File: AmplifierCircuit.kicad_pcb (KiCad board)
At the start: 2 copper layers, 69 x 38 mm, 29 parts

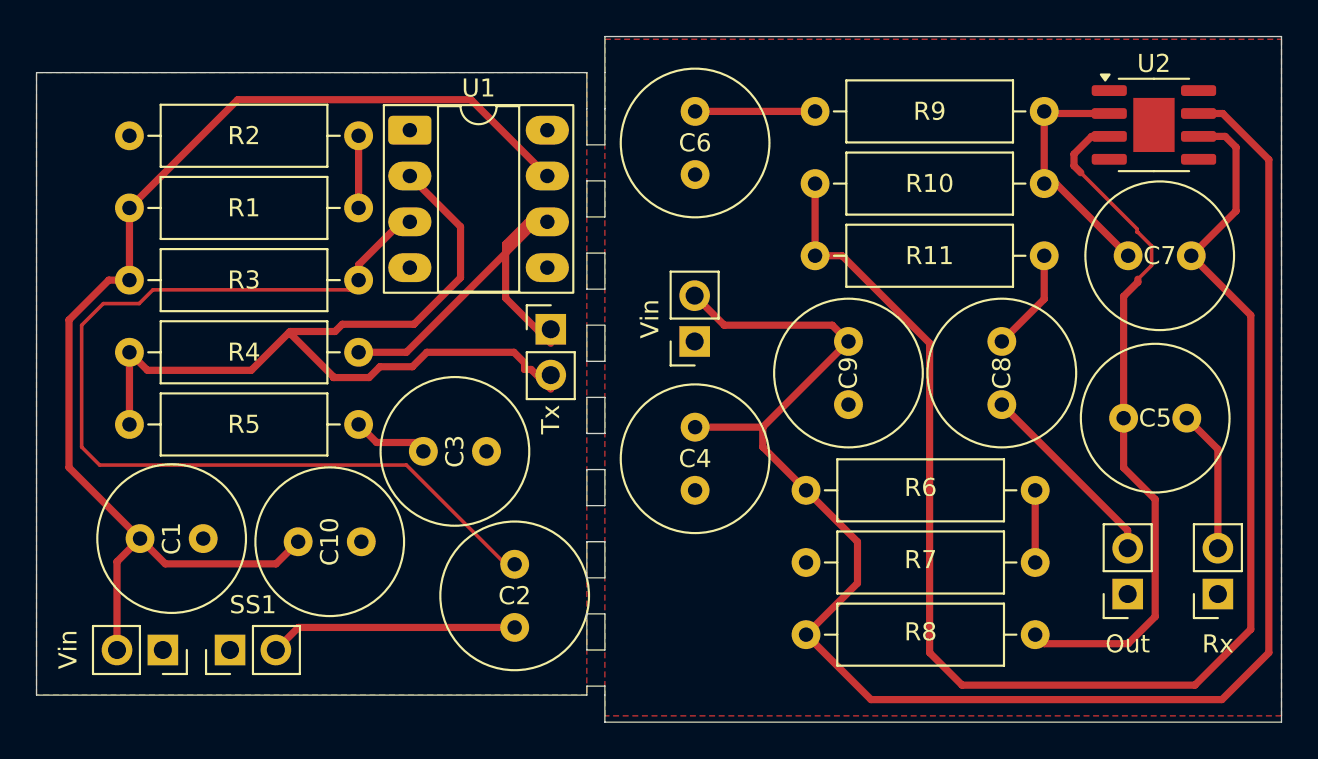
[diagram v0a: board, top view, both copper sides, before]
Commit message: Updated the footprints for SMD
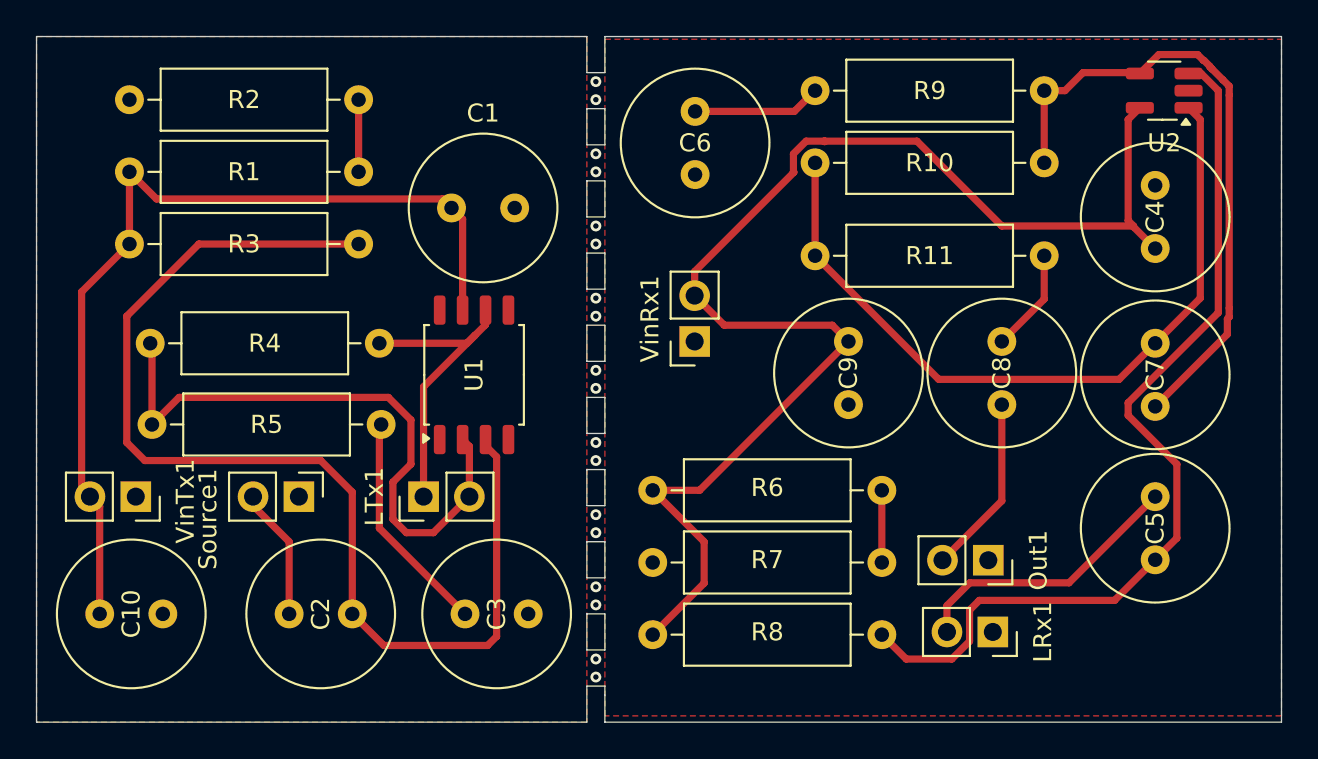
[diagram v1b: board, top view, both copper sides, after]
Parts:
- U1: footprint Package_DIP:DIP-8_W7.62mm_Socket_LongPads -> Package_SO:SOIC-8_5.3x5.3mm_P1.27mm
- U2: footprint Package_SO:SOIC-8-1EP_3.9x4.9mm_P1.27mm_EP2.29x3mm -> Package_TO_SOT_SMD:SOT-23-5_HandSoldering
- moved C4 27.4 mm to (111.5, 44.8), turned to 90 degrees
- moved C1 25.2 mm to (72.5, 42.5)
- moved U1 14.0 mm to (73.8, 51.8), turned to 90 degrees
- moved LRx1 12.7 mm to (102.5, 66.0), turned to -90 degrees
- moved C10 11.7 mm to (53.0, 65.0)
- moved LTx1 11.7 mm to (71.0, 58.5), turned to 90 degrees
- moved C2 9.41 mm to (67.0, 65.0), turned to 180 degrees
- moved Source1 9.32 mm to (64.0, 58.5), turned to -90 degrees
- moved C3 9.30 mm to (73.2, 65.0)
- moved VinTx1 8.63 mm to (55.0, 58.5)
- moved R6 8.50 mm to (83.7, 58.1)
- moved R7 8.50 mm to (96.3, 62.1)
- moved R8 8.50 mm to (83.7, 66.2)
- moved C5 8.04 mm to (111.5, 62.0), turned to 90 degrees
- moved Out1 7.95 mm to (102.2, 62.0), turned to -90 degrees
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- renumbered Rx to LRx1, Tx to LTx1, Out to Out1, SS1 to Source1, Vin to VinRx1, Vin to VinTx1
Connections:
- U2 pad 1: (no net) -> Net-(C7-Pad1)
- U2 pad 2: Net-(U2A--) -> GND2
- U2 pad 4: GND2 -> Net-(U2A--)
- U2 pad 5: (no net) -> VDD
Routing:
- net Net-(C7-Pad1): track 80.3 -> 42.0 mm
- net VDD: track 95.4 -> 74.2 mm
- net Net-(U2A--): track 14.5 -> 35.3 mm
- net VCC: track 66.0 -> 50.6 mm
- net Net-(LTx1-Pin_2): track 48.9 -> 34.6 mm
- net Net-(U2A-+): track 38.6 -> 50.7 mm
- net Net-(C3-Pad1): track 4.31 -> 12.5 mm
- net Net-(LRx1-Pin_2): track 7.92 -> 15.5 mm
- net Net-(U1A-+): track 54.5 -> 62.0 mm
- net Net-(Source1-Pin_2): track 13.8 -> 7.83 mm
- net Net-(LTx1-Pin_1): track 22.8 -> 17.2 mm
- net Net-(Out1-Pin_2): track 10.8 -> 9.99 mm
- net (no net): vias 0 -> 18
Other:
- outline, holes or cut-outs redrawn
